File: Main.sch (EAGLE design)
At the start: 13 parts, among them U1 ESP32-DEVKITC-32D

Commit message: esp32 footprint changed
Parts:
- U1: device ESP32-DEVKITC-32D:ESP32-DEVKITC-32D -> custom:ESP32-DEVKITC-32D
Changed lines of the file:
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@@
 <?xml version="1.0" encoding="utf-8"?>
 <!DOCTYPE eagle SYSTEM "eagle.dtd">
-<eagle version="9.5.2">
+<eagle version="9.6.0">
 <drawing>
 <settings>
@@
 <part name="R6" library="Resistor" deviceset="R" device="CHIP-0603(1608-METRIC)" package3d_urn="urn:adsk.eagle:package:16378565/1" technology="_"/>
 <part name="SUPPLY6" library="Power_Symbols" deviceset="GND" device=""/>
-<part name="U1" library="ESP32-DEVKITC-32D" deviceset="ESP32-DEVKITC-32D" device=""/>
+<part name="U1" library="custom" deviceset="ESP32-DEVKITC-32D" device=""/>
 <part name="CON1" library="con-harting" library_urn="urn:adsk.eagle:library:151" deviceset="CON10" device="" package3d_urn="urn:adsk.eagle:package:7121/1"/>
 <part name="JP1" library="pinhead" library_urn="urn:adsk.eagle:library:325" deviceset="PINHD-1X3" device="" package3d_urn="urn:adsk.eagle:package:22458/2"/>

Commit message: waiting for review
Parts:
- renumbered LORA_CONNECTED to LORA, MOVEMENT to MV, TIMEOUT to TOUT
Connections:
- net LORA_CLK: now also U1.IO18; no longer U1.IO14
- net LORA_CS: now also U1.IO5; no longer U1.IO15
- net LORA_DIO0: now also U1.IO21; no longer U1.IO2
- net LORA_LED: now also U1.IO33; no longer U1.IO25
- net LORA_MISO: now also U1.IO19; no longer U1.IO12
- net LORA_MOSI: now also U1.IO23; no longer U1.IO13
- net LORA_RST: now also U1.IO22; no longer U1.IO18
- net M_DIR1: now also U1.IO4; no longer U1.IO16
- net M_DIR2: now also U1.IO17; no longer U1.IO0
- net M_M0: now also U1.IO12; no longer U1.IO21
- net M_M1: now also U1.IO27; no longer U1.IO19
- net M_M2: now also U1.IO14; no longer U1.IO5
- net M_STEP1: now also U1.IO0; no longer U1.IO17
- net M_STEP2: now also U1.IO16; no longer U1.IO4
- net SERVO_1: now also U1.IO25; no longer U1.IO23
- net SERVO_2: now also U1.IO26; no longer U1.IO22
- net TIMEOUT_LED: now also U1.IO32; no longer U1.IO26
- net WS_LED: now also U1.IO35; no longer U1.IO27

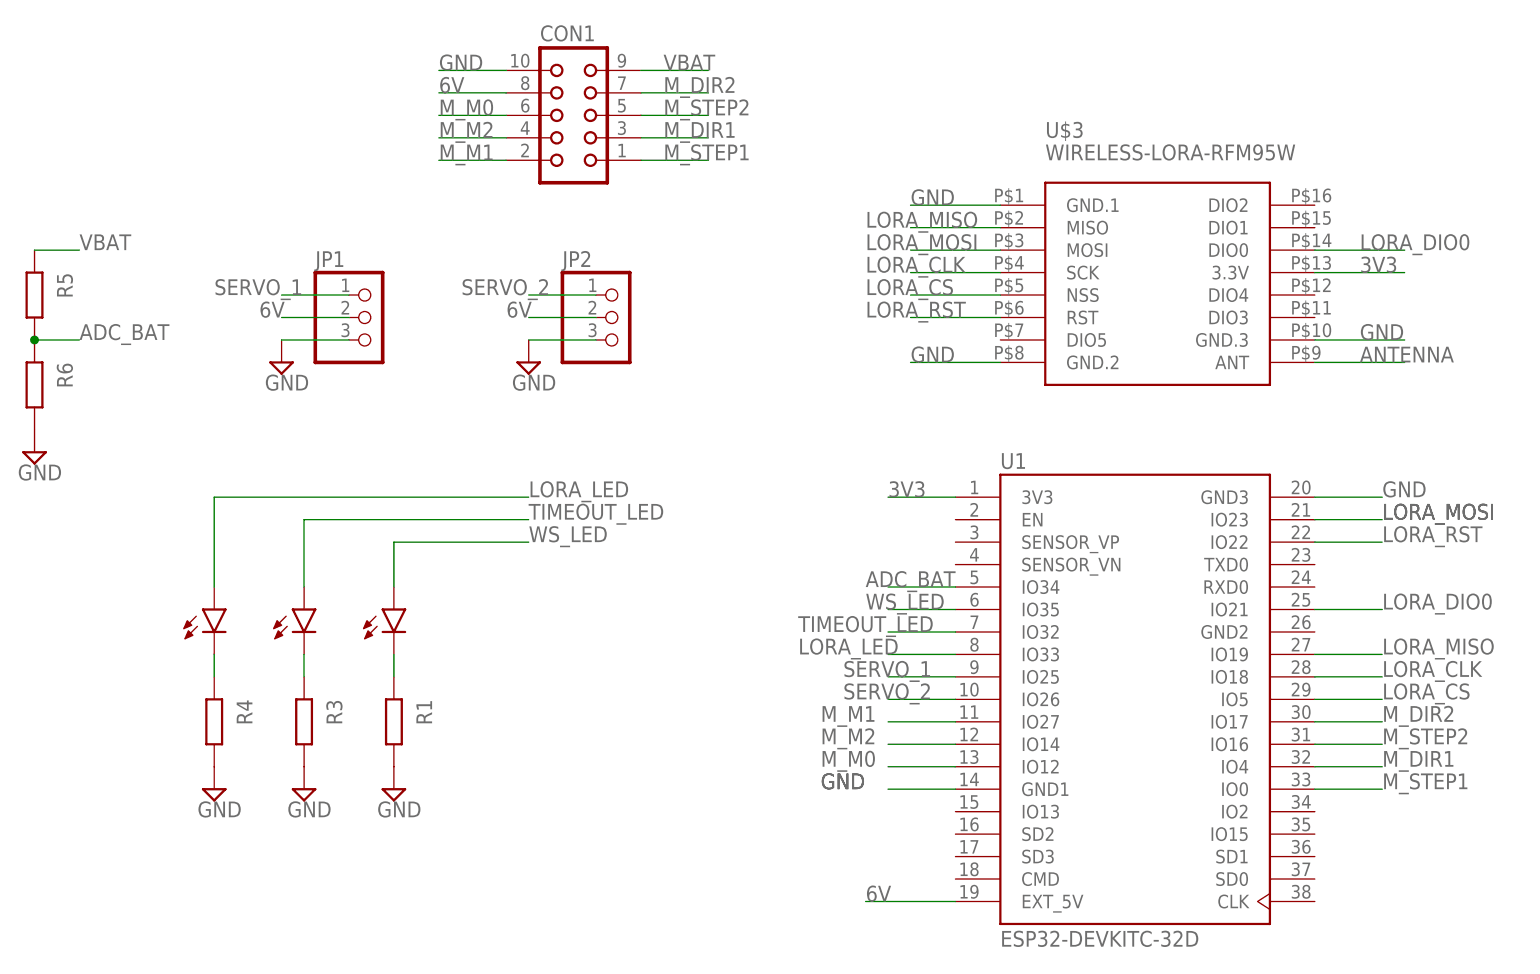
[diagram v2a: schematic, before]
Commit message: panel size fixed, fixing points added
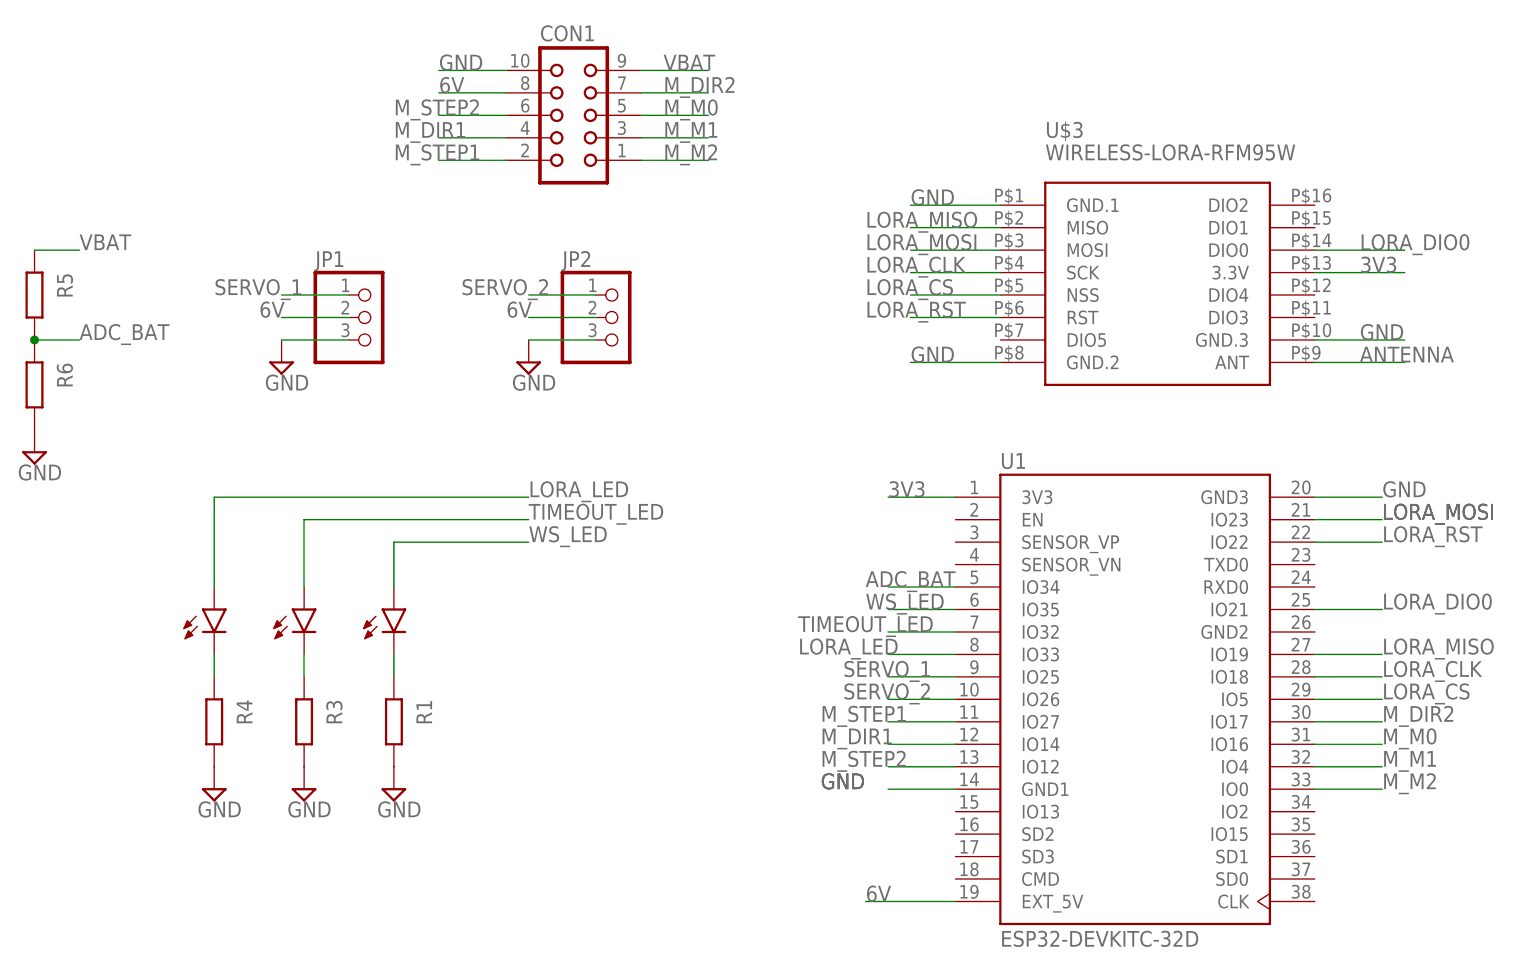
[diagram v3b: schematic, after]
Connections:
- net M_DIR1: now also CON1.4, U1.IO14; no longer CON1.3, U1.IO4
- net M_M0: now also CON1.5, U1.IO16; no longer CON1.6, U1.IO12
- net M_M1: now also CON1.3, U1.IO4; no longer CON1.2, U1.IO27
- net M_M2: now also CON1.1, U1.IO0; no longer CON1.4, U1.IO14
- net M_STEP1: now also CON1.2, U1.IO27; no longer CON1.1, U1.IO0
- net M_STEP2: now also CON1.6, U1.IO12; no longer CON1.5, U1.IO16
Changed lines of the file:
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@@
-</segment>
-</net>
-<net name="M_STEP1" class="0">
-<segment>
-<pinref part="CON1" gate="G$1" pin="1"/>
-<wire x1="-33.02" y1="111.76" x2="-25.4" y2="111.76" width="0.1524" layer="91"/>
-<label x="-30.48" y="111.76" size="1.778" layer="95"/>
-</segment>
-<segment>
-<pinref part="U1" gate="G$1" pin="IO0"/>
-<wire x1="43.18" y1="40.64" x2="50.8" y2="40.64" width="0.1524" layer="91"/>
-<label x="50.8" y="40.64" size="1.778" layer="95"/>
-</segment>
-</net>
-<net name="M_DIR1" class="0">
-<segment>
-<pinref part="CON1" gate="G$1" pin="3"/>
-<wire x1="-33.02" y1="114.3" x2="-25.4" y2="114.3" width="0.1524" layer="91"/>
-<label x="-30.48" y="114.3" size="1.778" layer="95"/>
-</segment>
-<segment>
-<pinref part="U1" gate="G$1" pin="IO4"/>
-<wire x1="43.18" y1="43.18" x2="50.8" y2="43.18" width="0.1524" layer="91"/>
-<label x="50.8" y="43.18" size="1.778" layer="95"/>
-</segment>
-</net>
-<net name="M_STEP2" class="0">
-<segment>
-<pinref part="CON1" gate="G$1" pin="5"/>
-<wire x1="-33.02" y1="116.84" x2="-25.4" y2="116.84" width="0.1524" layer="91"/>
-<label x="-30.48" y="116.84" size="1.778" layer="95"/>
-</segment>
-<segment>
-<pinref part="U1" gate="G$1" pin="IO16"/>
-<wire x1="43.18" y1="45.72" x2="50.8" y2="45.72" width="0.1524" layer="91"/>
-<label x="50.8" y="45.72" size="1.778" layer="95"/>
 </segment>
 </net>
@@
 <net name="M_M0" class="0">
 <segment>
-<pinref part="CON1" gate="G$1" pin="6"/>
-<wire x1="-48.26" y1="116.84" x2="-55.88" y2="116.84" width="0.1524" layer="91"/>
-<label x="-55.88" y="116.84" size="1.778" layer="95"/>
+<pinref part="U1" gate="G$1" pin="IO16"/>
+<wire x1="43.18" y1="45.72" x2="50.8" y2="45.72" width="0.1524" layer="91"/>
+<label x="50.8" y="45.72" size="1.778" layer="95"/>
 </segment>
 <segment>
-<pinref part="U1" gate="G$1" pin="IO12"/>
-<wire x1="2.54" y1="43.18" x2="-5.08" y2="43.18" width="0.1524" layer="91"/>
-<label x="-12.7" y="43.18" size="1.778" layer="95"/>
+<pinref part="CON1" gate="G$1" pin="5"/>
+<wire x1="-33.02" y1="116.84" x2="-25.4" y2="116.84" width="0.1524" layer="91"/>
+<label x="-30.48" y="116.84" size="1.778" layer="95"/>
 </segment>
 </net>
 <net name="M_M1" class="0">
 <segment>
-<pinref part="CON1" gate="G$1" pin="2"/>
-<wire x1="-48.26" y1="111.76" x2="-55.88" y2="111.76" width="0.1524" layer="91"/>
-<label x="-55.88" y="111.76" size="1.778" layer="95"/>
+<pinref part="CON1" gate="G$1" pin="3"/>
+<wire x1="-33.02" y1="114.3" x2="-25.4" y2="114.3" width="0.1524" layer="91"/>
+<label x="-30.48" y="114.3" size="1.778" layer="95"/>
 </segment>
 <segment>
-<pinref part="U1" gate="G$1" pin="IO27"/>
-<wire x1="2.54" y1="48.26" x2="-5.08" y2="48.26" width="0.1524" layer="91"/>
-<label x="-12.7" y="48.26" size="1.778" layer="95"/>
+<pinref part="U1" gate="G$1" pin="IO4"/>
+<wire x1="43.18" y1="43.18" x2="50.8" y2="43.18" width="0.1524" layer="91"/>
+<label x="50.8" y="43.18" size="1.778" layer="95"/>
 </segment>
 </net>
 <net name="M_M2" class="0">
 <segment>
-<pinref part="CON1" gate="G$1" pin="4"/>
-<wire x1="-48.26" y1="114.3" x2="-55.88" y2="114.3" width="0.1524" layer="91"/>
-<label x="-55.88" y="114.3" size="1.778" layer="95"/>
+<pinref part="CON1" gate="G$1" pin="1"/>
+<wire x1="-33.02" y1="111.76" x2="-25.4" y2="111.76" width="0.1524" layer="91"/>
+<label x="-30.48" y="111.76" size="1.778" layer="95"/>
 </segment>
 <segment>
-<pinref part="U1" gate="G$1" pin="IO14"/>
-<wire x1="2.54" y1="45.72" x2="-5.08" y2="45.72" width="0.1524" layer="91"/>
-<label x="-12.7" y="45.72" size="1.778" layer="95"/>
+<pinref part="U1" gate="G$1" pin="IO0"/>
+<wire x1="43.18" y1="40.64" x2="50.8" y2="40.64" width="0.1524" layer="91"/>
+<label x="50.8" y="40.64" size="1.778" layer="95"/>
 </segment>
 </net>
@@
 </segment>
 </net>
+<net name="M_STEP1" class="0">
+<segment>
+<pinref part="CON1" gate="G$1" pin="2"/>
+<wire x1="-48.26" y1="111.76" x2="-55.88" y2="111.76" width="0.1524" layer="91"/>
+<label x="-60.96" y="111.76" size="1.778" layer="95"/>
+</segment>
+<segment>
+<pinref part="U1" gate="G$1" pin="IO27"/>
+<wire x1="2.54" y1="48.26" x2="-5.08" y2="48.26" width="0.1524" layer="91"/>
+<label x="-12.7" y="48.26" size="1.778" layer="95"/>
+</segment>
+</net>
+<net name="M_DIR1" class="0">
+<segment>
+<pinref part="U1" gate="G$1" pin="IO14"/>
+<wire x1="2.54" y1="45.72" x2="-5.08" y2="45.72" width="0.1524" layer="91"/>
+<label x="-12.7" y="45.72" size="1.778" layer="95"/>
+</segment>
+<segment>
+<pinref part="CON1" gate="G$1" pin="4"/>
+<wire x1="-48.26" y1="114.3" x2="-55.88" y2="114.3" width="0.1524" layer="91"/>
+<label x="-60.96" y="114.3" size="1.778" layer="95"/>
+</segment>
+</net>
+<net name="M_STEP2" class="0">
+<segment>
+<pinref part="CON1" gate="G$1" pin="6"/>
+<wire x1="-48.26" y1="116.84" x2="-55.88" y2="116.84" width="0.1524" layer="91"/>
+<label x="-60.96" y="116.84" size="1.778" layer="95"/>
+</segment>
+<segment>
+<pinref part="U1" gate="G$1" pin="IO12"/>
+<wire x1="2.54" y1="43.18" x2="-5.08" y2="43.18" width="0.1524" layer="91"/>
+<label x="-12.7" y="43.18" size="1.778" layer="95"/>
+</segment>
+</net>
